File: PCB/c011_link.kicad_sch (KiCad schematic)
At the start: 8 parts, among them J1 Conn_02x20_Odd_Even, J2 Conn_01x07, U1 C011, U2 TXS0108EPW_DIP20, U3 TXS0108EPW_DIP20, X1 CXO_DIP14

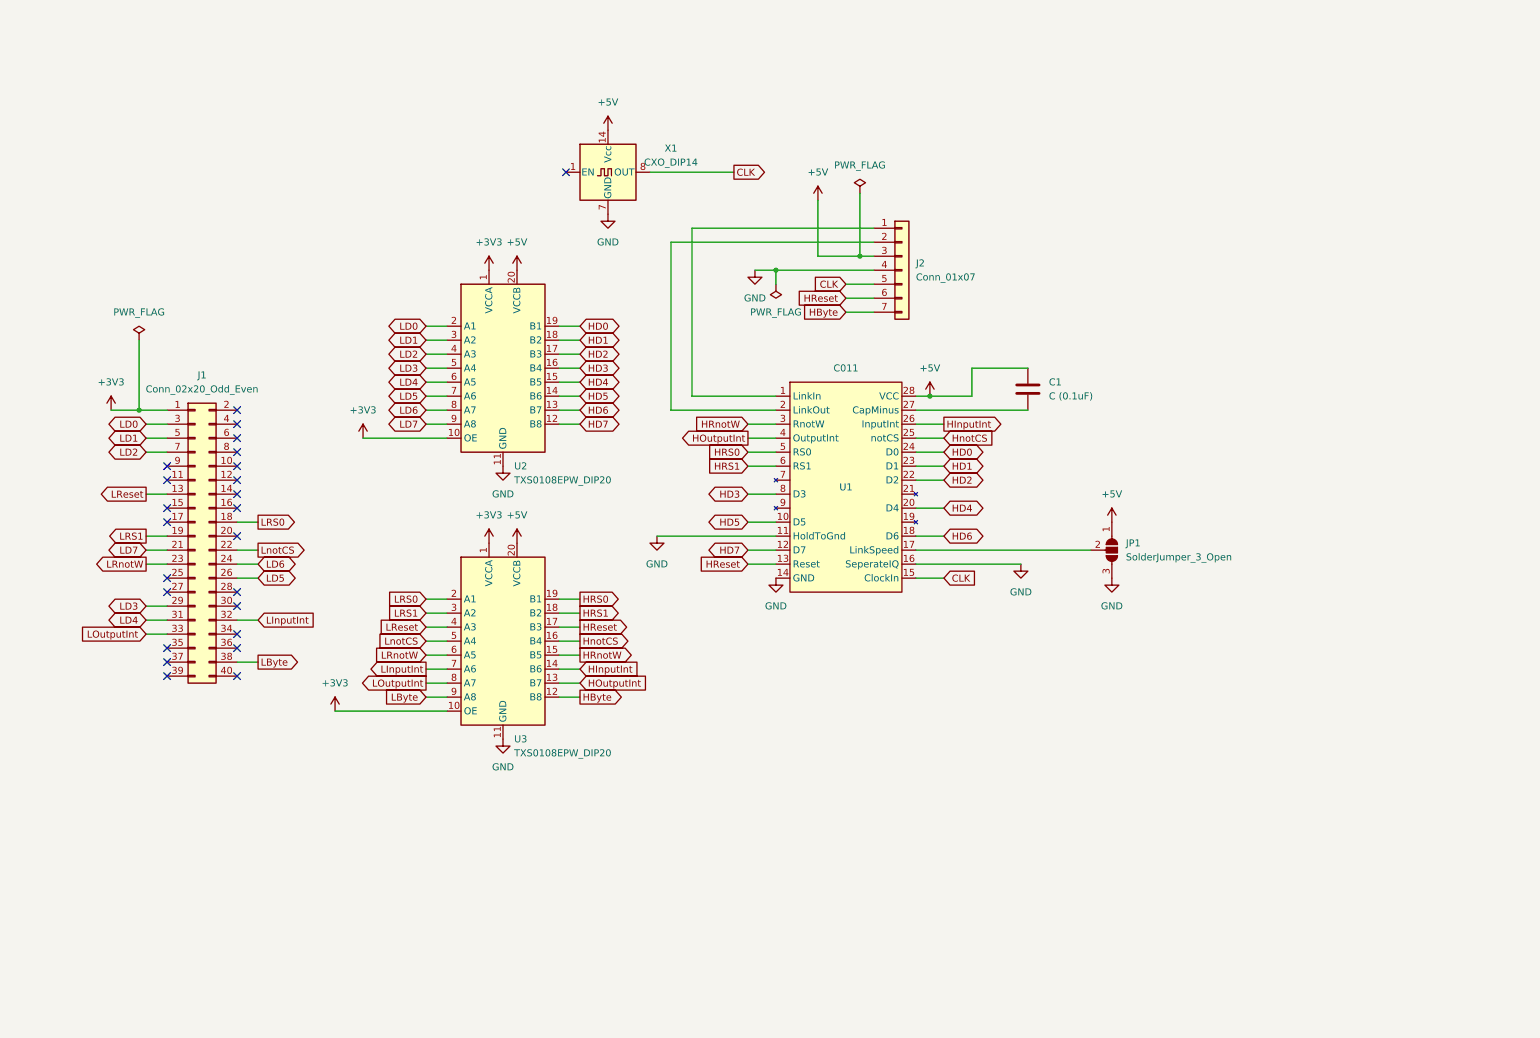
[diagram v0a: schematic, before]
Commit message: Update to PCB 1.1 design
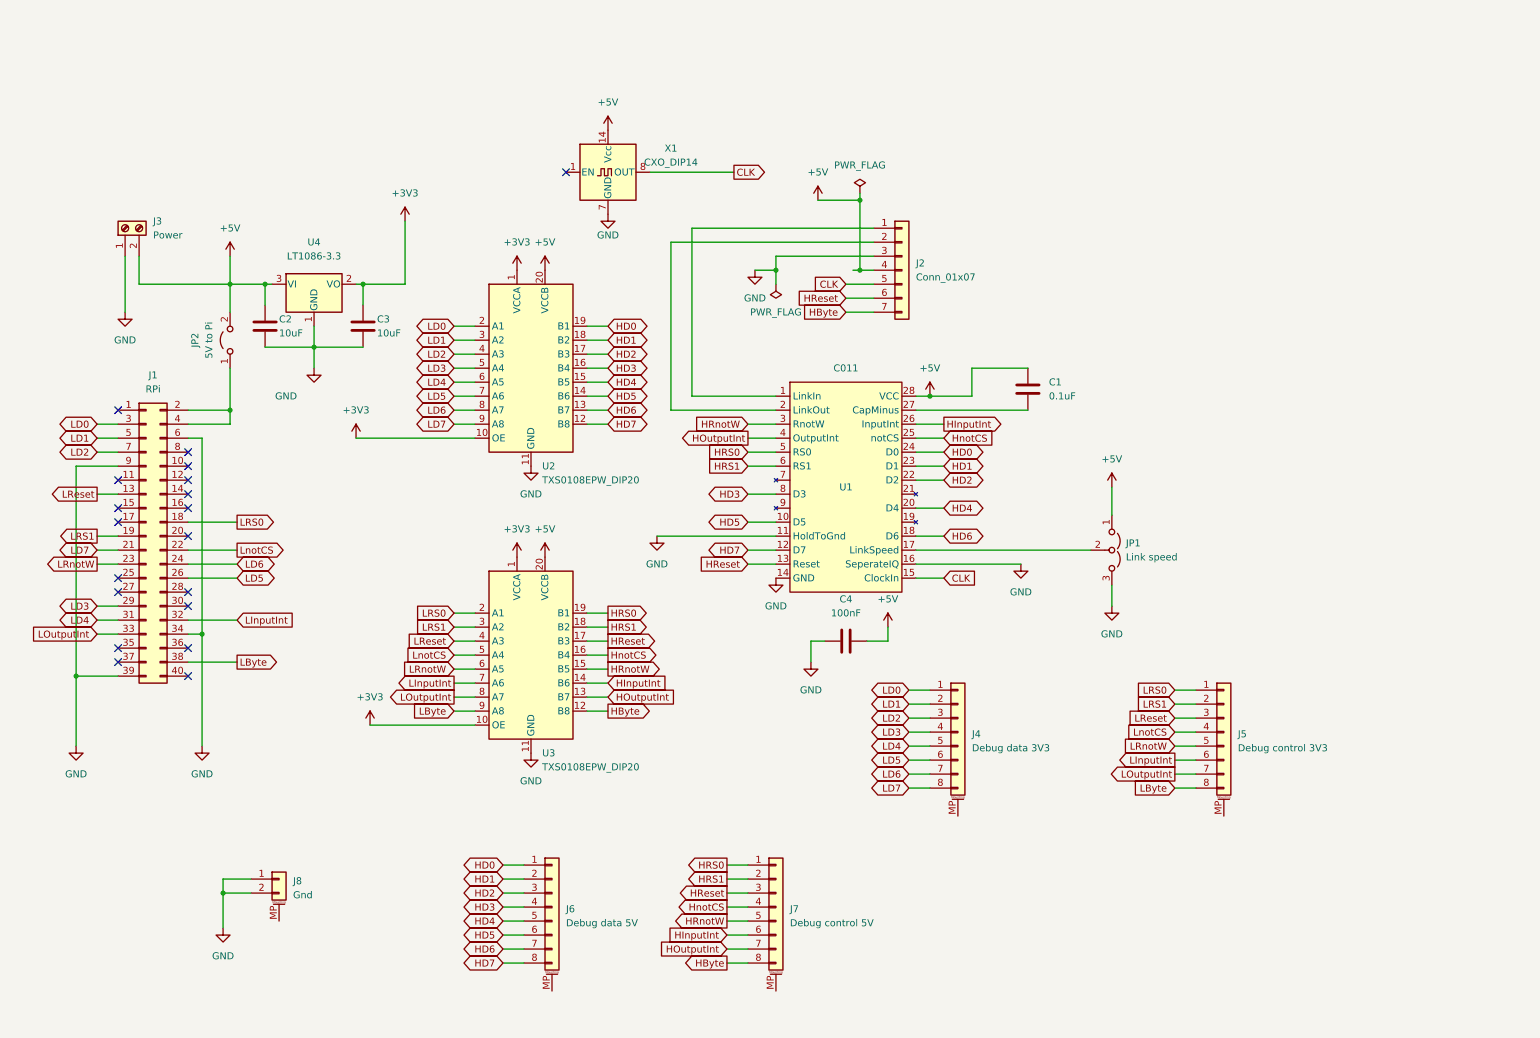
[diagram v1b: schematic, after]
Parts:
- removed JP1: SolderJumper_3_Open, Jumper:SolderJumper-3_P2.0mm_Open_TrianglePad1.0x1.5mm, symbol Jumper:SolderJumper_3_Open
- added C2, C3: 10uF, Capacitor_THT:CP_Radial_Tantal_D5.0mm_P2.50mm, symbol Device:C
- added C4: 100nF, Capacitor_THT:C_Disc_D5.0mm_W2.5mm_P2.50mm, symbol Device:C
- added J3: Power, TerminalBlock:TerminalBlock_bornier-2_P5.08mm, symbol Connector:Screw_Terminal_01x02
- added J4: Debug data 3V3, Connector_PinHeader_2.54mm:PinHeader_1x08_P2.54mm_Vertical, symbol Connector_Generic_MountingPin:Conn_01x08_MountingPin
- added J5: Debug control 3V3, Connector_PinHeader_2.54mm:PinHeader_1x08_P2.54mm_Vertical, symbol Connector_Generic_MountingPin:Conn_01x08_MountingPin
- added J6: Debug data 5V, Connector_PinHeader_2.54mm:PinHeader_1x08_P2.54mm_Vertical, symbol Connector_Generic_MountingPin:Conn_01x08_MountingPin
- added J7: Debug control 5V, Connector_PinHeader_2.54mm:PinHeader_1x08_P2.54mm_Vertical, symbol Connector_Generic_MountingPin:Conn_01x08_MountingPin
- added J8: Gnd, Connector_PinHeader_2.54mm:PinHeader_1x02_P2.54mm_Vertical, symbol Connector_Generic_MountingPin:Conn_01x02_MountingPin
- added JP1: Link speed, Connector_PinHeader_2.54mm:PinHeader_1x03_P2.54mm_Vertical, symbol Jumper:Jumper_3_Open
- added JP2: 5V to Pi, Connector_PinHeader_2.54mm:PinHeader_1x02_P2.54mm_Vertical, symbol Jumper:Jumper_2_Open
- added U4: LT1086-3.3, Package_TO_SOT_THT:TO-220-3_Horizontal_TabDown, symbol Regulator_Linear:LT1086-3.3
- C1: value C (0.1uF) -> 0.1uF
- J1: value Conn_02x20_Odd_Even -> RPi
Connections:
- net +3V3: now also C3.1, U4.2 (VO); no longer J1.1 (Pin_1)
- net +5V: now also J2.4 (Pin_4), C2.1, C4.1, J3.2 (Pin_2), JP1.1 (A), JP2.2 (B), U4.3 (VI); no longer J2.3 (Pin_3)
- net GND: now also J1.34 (Pin_34), J1.39 (Pin_39), J1.6 (Pin_6), J1.9 (Pin_9), J2.3 (Pin_3), C2.2, C3.2, C4.2, J3.1 (Pin_1), J8.1 (Pin_1), J8.2 (Pin_2), JP1.3 (B), U4.1 (GND); no longer J2.4 (Pin_4)
- net HByte: now also J7.8 (Pin_8)
- net HD0: now also J6.1 (Pin_1)
- net HD1: now also J6.2 (Pin_2)
- net HD2: now also J6.3 (Pin_3)
- net HD3: now also J6.4 (Pin_4)
- net HD4: now also J6.5 (Pin_5)
- net HD5: now also J6.6 (Pin_6)
- net HD6: now also J6.7 (Pin_7)
- net HD7: now also J6.8 (Pin_8)
- net HInputInt: now also J7.6 (Pin_6)
- net HOutputInt: now also J7.7 (Pin_7)
- net HRS0: now also J7.1 (Pin_1)
- net HRS1: now also J7.2 (Pin_2)
- net HReset: now also J7.3 (Pin_3)
- net HRnotW: now also J7.5 (Pin_5)
- net HnotCS: now also J7.4 (Pin_4)
- net LByte: now also J5.8 (Pin_8)
- net LD0: now also J4.1 (Pin_1)
- net LD1: now also J4.2 (Pin_2)
- net LD2: now also J4.3 (Pin_3)
- net LD3: now also J4.4 (Pin_4)
- net LD4: now also J4.5 (Pin_5)
- net LD5: now also J4.6 (Pin_6)
- net LD6: now also J4.7 (Pin_7)
- net LD7: now also J4.8 (Pin_8)
- net LInputInt: now also J5.6 (Pin_6)
- net LOutputInt: now also J5.7 (Pin_7)
- net LRS0: now also J5.1 (Pin_1)
- net LRS1: now also J5.2 (Pin_2)
- net LReset: now also J5.3 (Pin_3)
- net LRnotW: now also J5.5 (Pin_5)
- net LnotCS: now also J5.4 (Pin_4)
- net at U1.17 (LinkSpeed): now also JP1.2 (C)
- net at J1.2 (Pin_2): now also J1.4 (Pin_4), JP2.1 (A)
- no-connect marks 24 -> 19
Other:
- moved on the sheet: J1, U2, U3

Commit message: move to 74LVC8T245 level converters
The existing auto detecting direction shifters can glitch into the 'wrong' direction
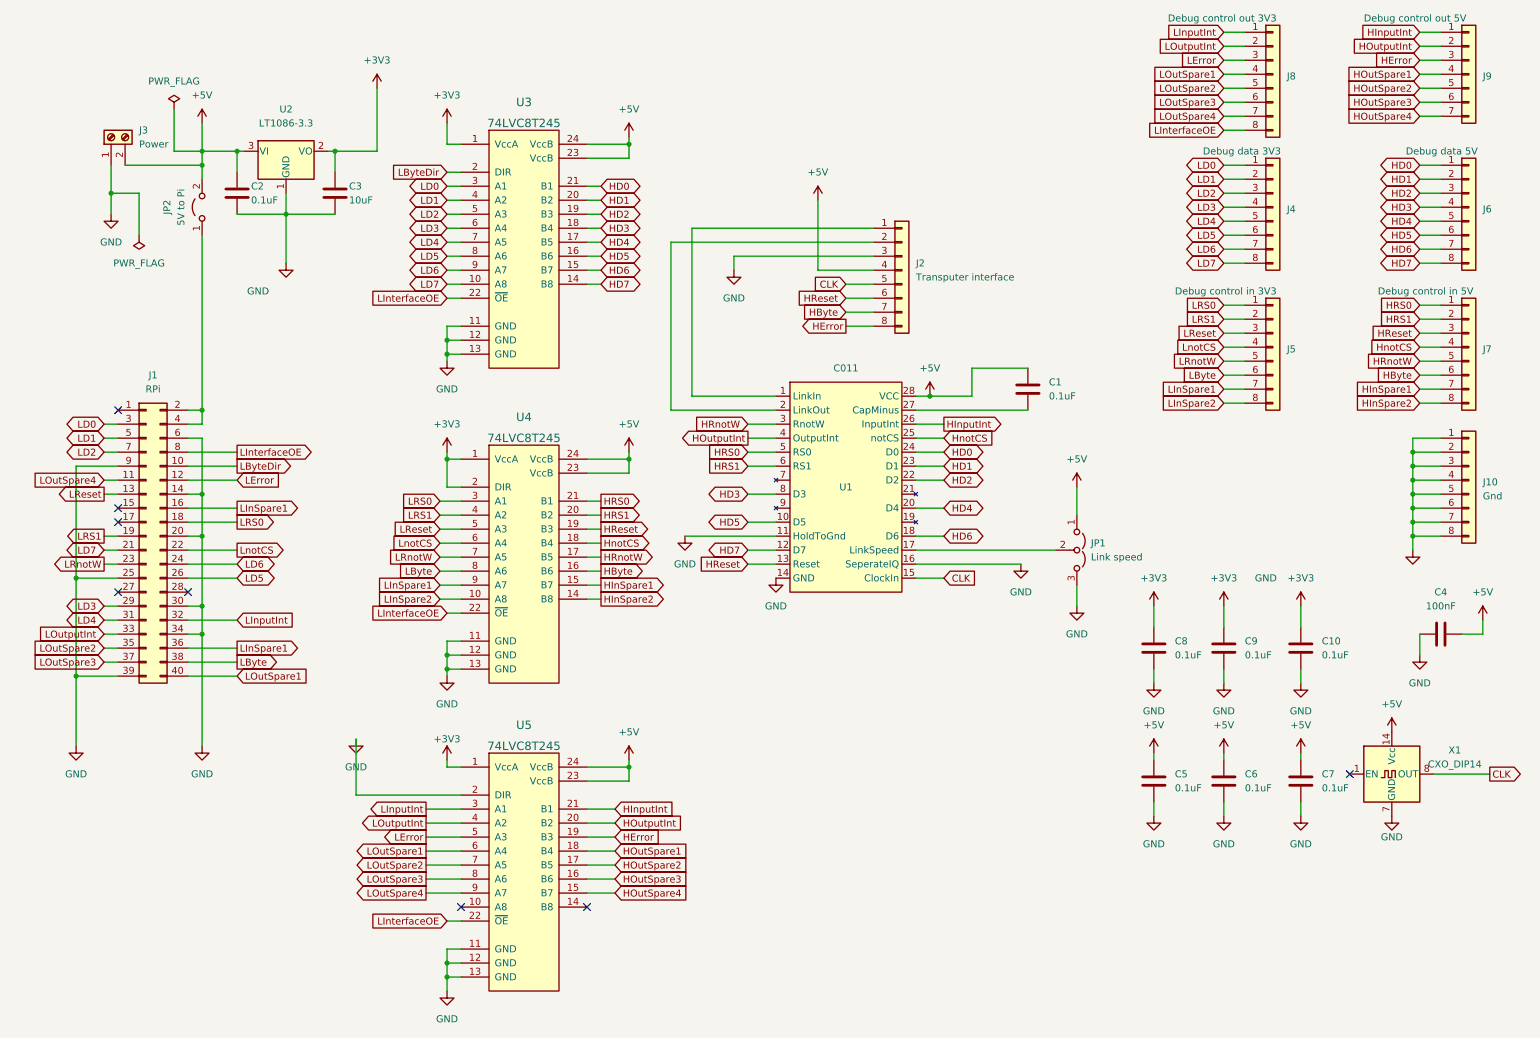
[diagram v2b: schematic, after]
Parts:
- removed U2, U3: TXS0108EPW_DIP20, Package_DIP:DIP-20_W12.7mm, symbol Logic_LevelTranslator:TXS0108EPW_DIP20
- added C10, C5, C6, C7, C8, C9: 0.1uF, Capacitor_SMD:C_0402_1005Metric_Pad0.74x0.62mm_HandSolder, symbol Device:C
- added J8: Debug control out 3V3, Connector_PinHeader_2.54mm:PinHeader_1x08_P2.54mm_Vertical, symbol Connector_Generic:Conn_01x08
- added J9: Debug control out 5V, Connector_PinHeader_2.54mm:PinHeader_1x07_P2.54mm_Vertical, symbol Connector_Generic:Conn_01x07
- added U3, U4, U5: 74LVC8T245, Package_SO:SOIC-24W_7.5x15.4mm_P1.27mm, symbol Logic_LevelTranslator:74LVC8T245
- C2: value 10uF -> 0.1uF; footprint Capacitor_THT:CP_Radial_Tantal_D5.0mm_P2.50mm -> Capacitor_THT:C_Disc_D5.0mm_W2.5mm_P5.00mm
- C4: footprint Capacitor_THT:C_Disc_D5.0mm_W2.5mm_P2.50mm -> Capacitor_THT:C_Disc_D5.0mm_W2.5mm_P5.00mm
- J10: renamed from J8; footprint Connector_PinHeader_2.54mm:PinHeader_1x02_P2.54mm_Vertical -> Connector_PinHeader_2.54mm:PinHeader_1x08_P2.54mm_Vertical; symbol Connector_Generic_MountingPin:Conn_01x02_MountingPin -> Connector_Generic:Conn_01x08
- J2: value Conn_01x07 -> Transputer interface; footprint Connector_PinHeader_2.54mm:PinHeader_1x07_P2.54mm_Vertical -> Connector_PinHeader_2.54mm:PinHeader_1x08_P2.54mm_Vertical; symbol Connector_Generic:Conn_01x07 -> Connector_Generic:Conn_01x08
- J4, J6: symbol Connector_Generic_MountingPin:Conn_01x08_MountingPin -> Connector_Generic:Conn_01x08
- J5: value Debug control 3V3 -> Debug control in 3V3; symbol Connector_Generic_MountingPin:Conn_01x08_MountingPin -> Connector_Generic:Conn_01x08
- J7: value Debug control 5V -> Debug control in 5V; symbol Connector_Generic_MountingPin:Conn_01x08_MountingPin -> Connector_Generic:Conn_01x08
- renumbered U4 to U2
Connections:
- net +3V3: now also C10.1, C8.1, C9.1, U3.1 (VccA), U4.1 (VccA), U4.2 (DIR), U5.1 (VccA)
- net +5V: now also C5.1, C6.1, C7.1, U3.23 (VccB), U3.24 (VccB), U4.23 (VccB), U4.24 (VccB), U5.23 (VccB), U5.24 (VccB)
- net GND: now also J1.14 (Pin_14), J1.20 (Pin_20), J1.25 (Pin_25), J1.30 (Pin_30), J10.3 (Pin_3), J10.4 (Pin_4), J10.5 (Pin_5), J10.6 (Pin_6), J10.7 (Pin_7), J10.8 (Pin_8), C10.2, C5.2, C6.2, C7.2, C8.2, C9.2, U3.11 (GND), U3.12 (GND), U3.13 (GND), U4.11 (GND), U4.12 (GND), U4.13 (GND), U5.11 (GND), U5.12 (GND), U5.13 (GND), U5.2 (DIR)
- net HByte: now also J7.6 (Pin_6), U4.16 (B6); no longer J7.8 (Pin_8)
- net HD0: now also U3.21 (B1)
- net HD1: now also U3.20 (B2)
- net HD2: now also U3.19 (B3)
- net HD3: now also U3.18 (B4)
- net HD4: now also U3.17 (B5)
- net HD5: now also U3.16 (B6)
- net HD6: now also U3.15 (B7)
- net HD7: now also U3.14 (B8)
- net HInputInt: now also J9.1 (Pin_1), U5.21 (B1); no longer J7.6 (Pin_6)
- net HOutputInt: now also J9.2 (Pin_2), U5.20 (B2); no longer J7.7 (Pin_7)
- net HRS0: now also U4.21 (B1)
- net HRS1: now also U4.20 (B2)
- net HReset: now also U4.19 (B3)
- net HRnotW: now also U4.17 (B5)
- net HnotCS: now also U4.18 (B4)
- net LByte: now also J5.6 (Pin_6), U4.8 (A6); no longer J5.8 (Pin_8)
- net LD0: now also U3.3 (A1)
- net LD1: now also U3.4 (A2)
- net LD2: now also U3.5 (A3)
- net LD3: now also U3.6 (A4)
- net LD4: now also U3.7 (A5)
- net LD5: now also U3.8 (A6)
- net LD6: now also U3.9 (A7)
- net LD7: now also U3.10 (A8)
- net LInputInt: now also J8.1 (Pin_1), U5.3 (A1); no longer J5.6 (Pin_6)
- net LOutputInt: now also J8.2 (Pin_2), U5.4 (A2); no longer J5.7 (Pin_7)
- net LRS0: now also U4.3 (A1)
- net LRS1: now also U4.4 (A2)
- net LReset: now also U4.5 (A3)
- net LRnotW: now also U4.7 (A5)
- net LnotCS: now also U4.6 (A4)
- net LByteDir: now reaches J1.10 (Pin_10)
- net LByteDir: now also U3.2 (DIR)
- net LOutSpare4: now reaches J1.11 (Pin_11)
- net LOutSpare4: now also J8.7 (Pin_7), U5.9 (A7)
- net LError: now reaches J1.12 (Pin_12)
- net LError: now also J8.3 (Pin_3), U5.5 (A3)
- net LInSpare1: now reaches J1.16 (Pin_16)
- net LInSpare1: now also J1.36 (Pin_36), J5.7 (Pin_7), U4.9 (A7)
- net LOutSpare2: now reaches J1.35 (Pin_35)
- net LOutSpare2: now also J8.5 (Pin_5), U5.7 (A5)
- net LOutSpare3: now reaches J1.37 (Pin_37)
- net LOutSpare3: now also J8.6 (Pin_6), U5.8 (A6)
- net LOutSpare1: now reaches J1.40 (Pin_40)
- net LOutSpare1: now also J8.4 (Pin_4), U5.6 (A4)
- net LInterfaceOE: now reaches J1.8 (Pin_8)
- net LInterfaceOE: now also J8.8 (Pin_8), U3.22 (~{OE}), U4.22 (~{OE}), U5.22 (~{OE})
- new net HError: J2.8 (Pin_8), J9.3 (Pin_3), U5.19 (B3)
- new net HInSpare1: J7.7 (Pin_7), U4.15 (B7)
- new net HInSpare2: J7.8 (Pin_8), U4.14 (B8)
- new net HOutSpare1: J9.4 (Pin_4), U5.18 (B4)
- new net HOutSpare2: J9.5 (Pin_5), U5.17 (B5)
- new net HOutSpare3: J9.6 (Pin_6), U5.16 (B6)
- new net HOutSpare4: J9.7 (Pin_7), U5.15 (B7)
- new net LInSpare2: J5.8 (Pin_8), U4.10 (A8)
- no-connect marks 19 -> 8
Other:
- moved on the sheet: C2, C3, C4, J3, JP1, JP2, U2, X1
